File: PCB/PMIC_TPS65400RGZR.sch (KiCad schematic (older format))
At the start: 1 part

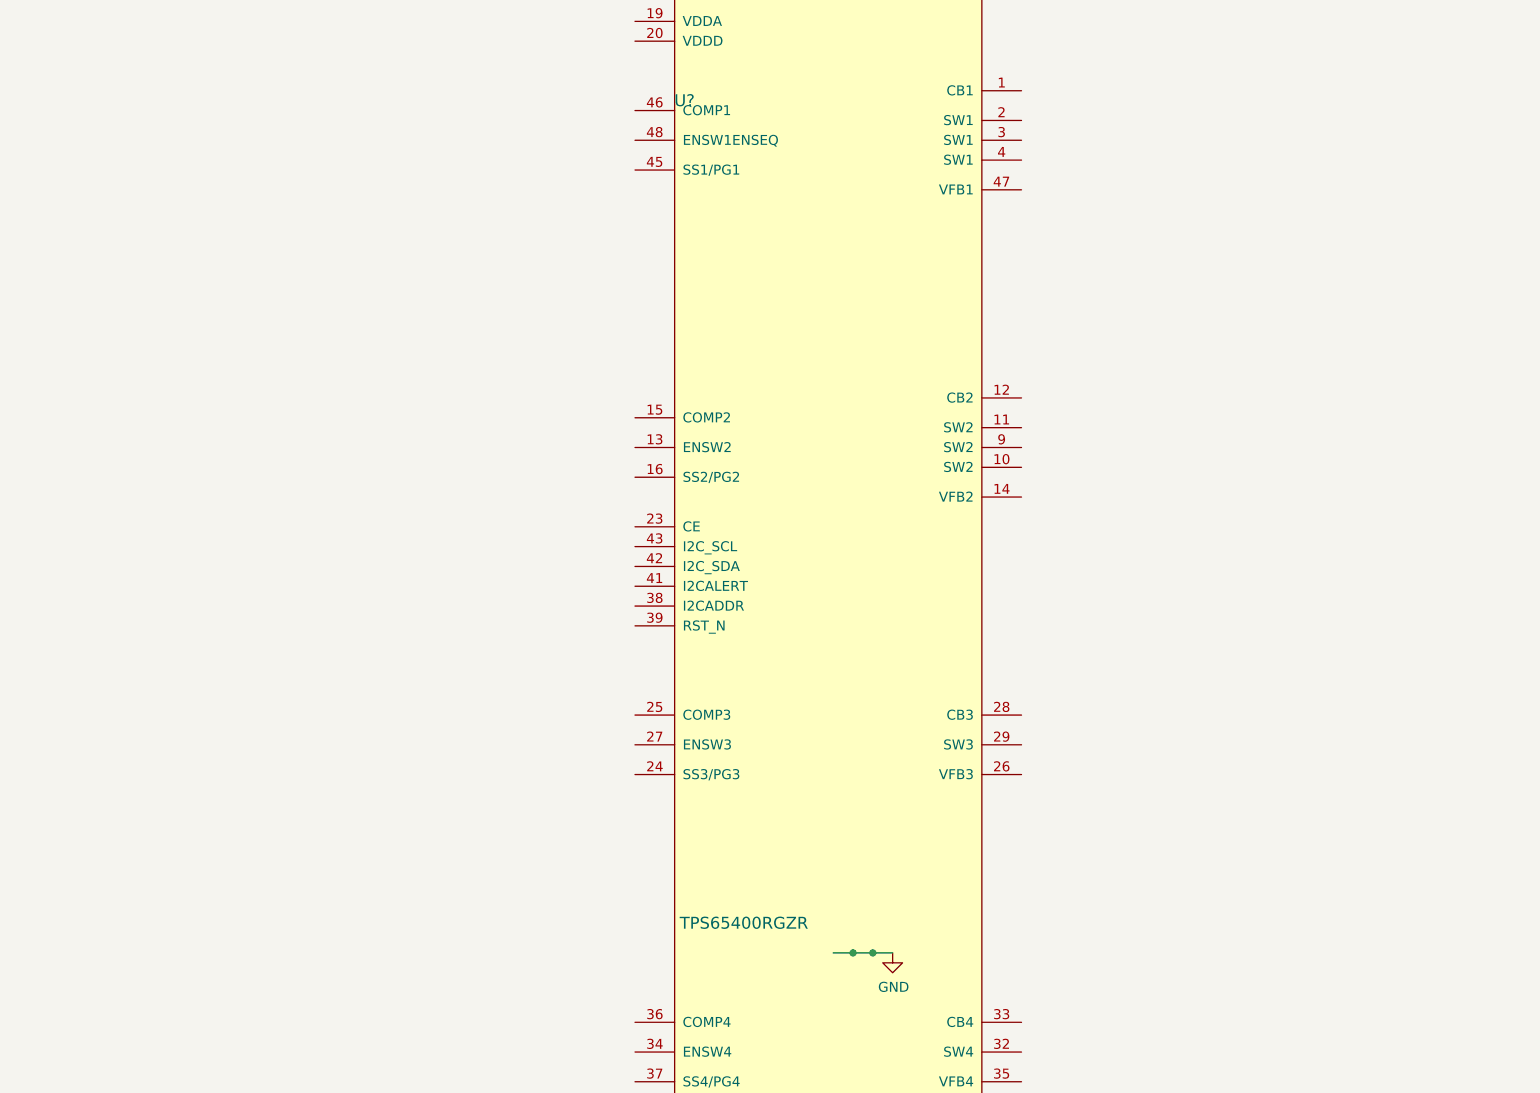
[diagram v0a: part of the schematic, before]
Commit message: PMIC progress
PMIC schematic implementation underway. will finish tomorrow evening
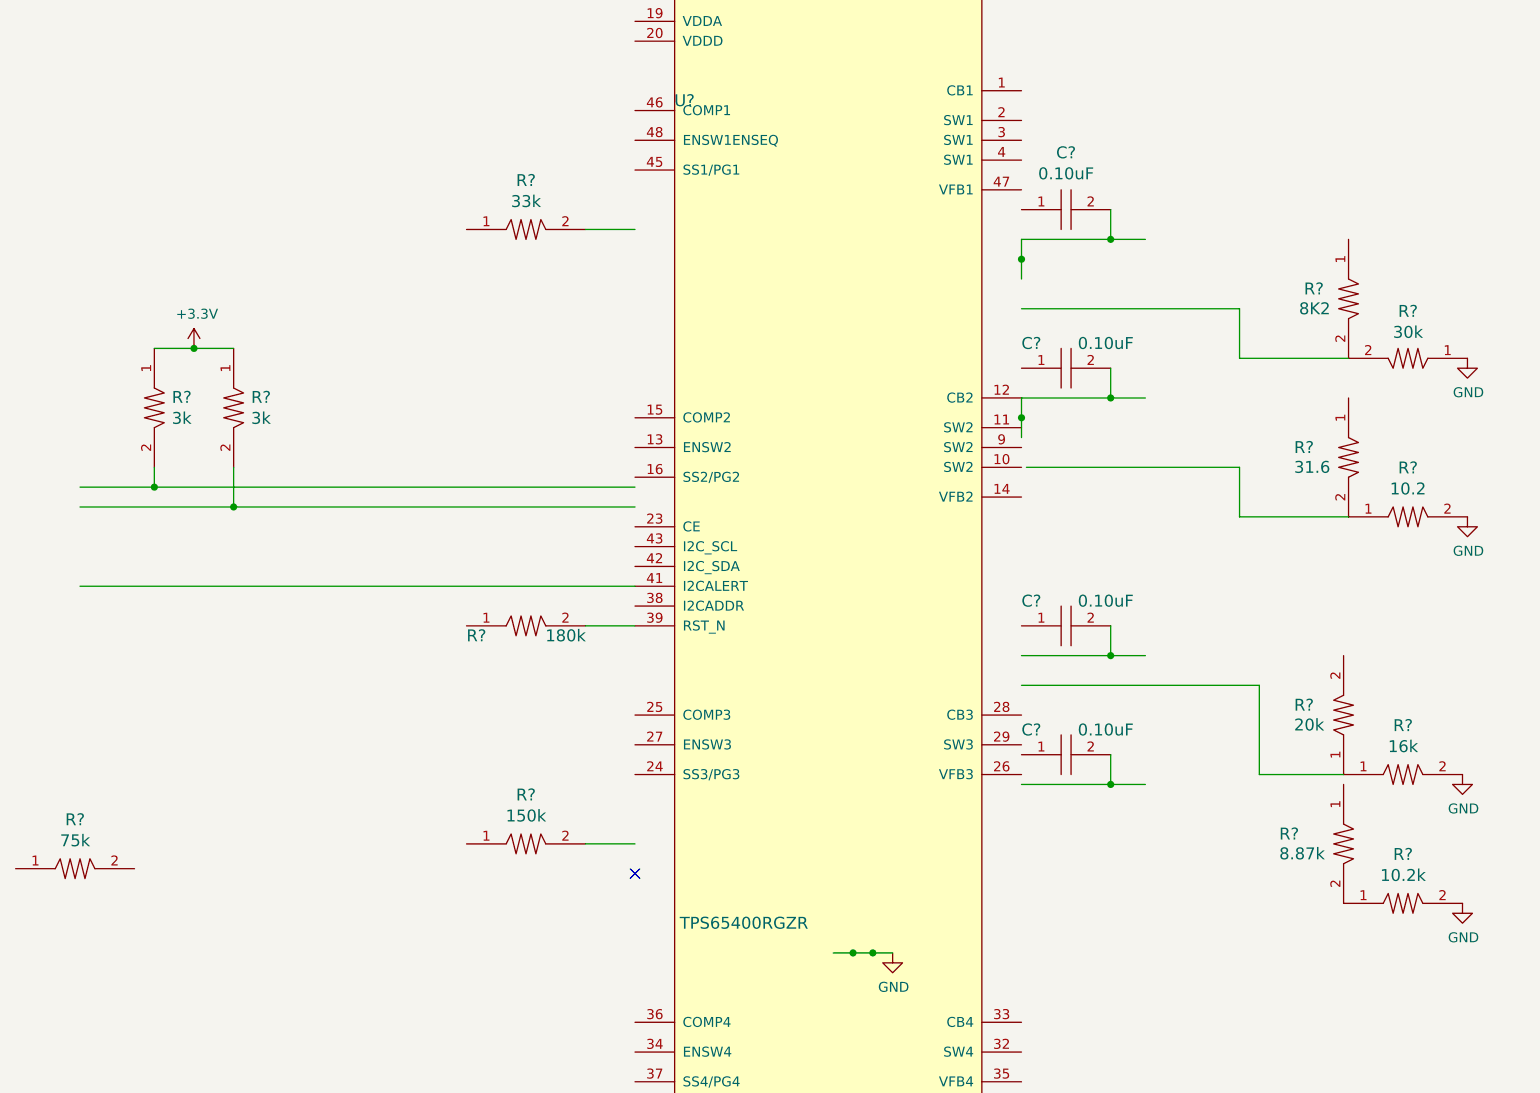
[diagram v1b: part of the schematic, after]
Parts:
- added C? (x4): CL05A104JO5NNNC, PCB_Footprints:C0402, symbol CL05A104JO5NNNC
- added R?: RC0402FR-0710K2L, PCB_Footprints:R0402, symbol RC0402FR-0710K2L
- added R?: RC0402FR-0710R2L, PCB_Footprints:R0402, symbol RC0402FR-0710R2L
- added R?: RC0402FR-07150KL, PCB_Footprints:R0402, symbol RC0402FR-07150KL
- added R?: RC0402FR-0716KL, PCB_Footprints:R0402, symbol RC0402FR-0716KL
- added R?: RC0402FR-07180KL, PCB_Footprints:R0402, symbol RC0402FR-07180KL
- added R?: RC0402FR-0720KL, PCB_Footprints:R0402, symbol RC0402FR-0720KL
- added R?: RC0402FR-0730KL, PCB_Footprints:R0402, symbol RC0402FR-0730KL
- added R?: RC0402FR-0731R6L, PCB_Footprints:R0402, symbol RC0402FR-0731R6L
- added R?: RC0402FR-0733KL, PCB_Footprints:R0402, symbol RC0402FR-0733KL
- added R? (x2): RC0402FR-073KL, PCB_Footprints:R0402, symbol RC0402FR-073KL
- added R?: RC0402FR-0775KL, PCB_Footprints:R0402, symbol RC0402FR-0775KL
- added R?: RC0402FR-078K2L, PCB_Footprints:R0402, symbol RC0402FR-078K2L
- added R?: RC0402FR-078K87L, PCB_Footprints:R0402, symbol RC0402FR-078K87L
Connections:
- net labels added: +3.3V
- wire segments 1 -> 39
- no-connect marks 0 -> 1

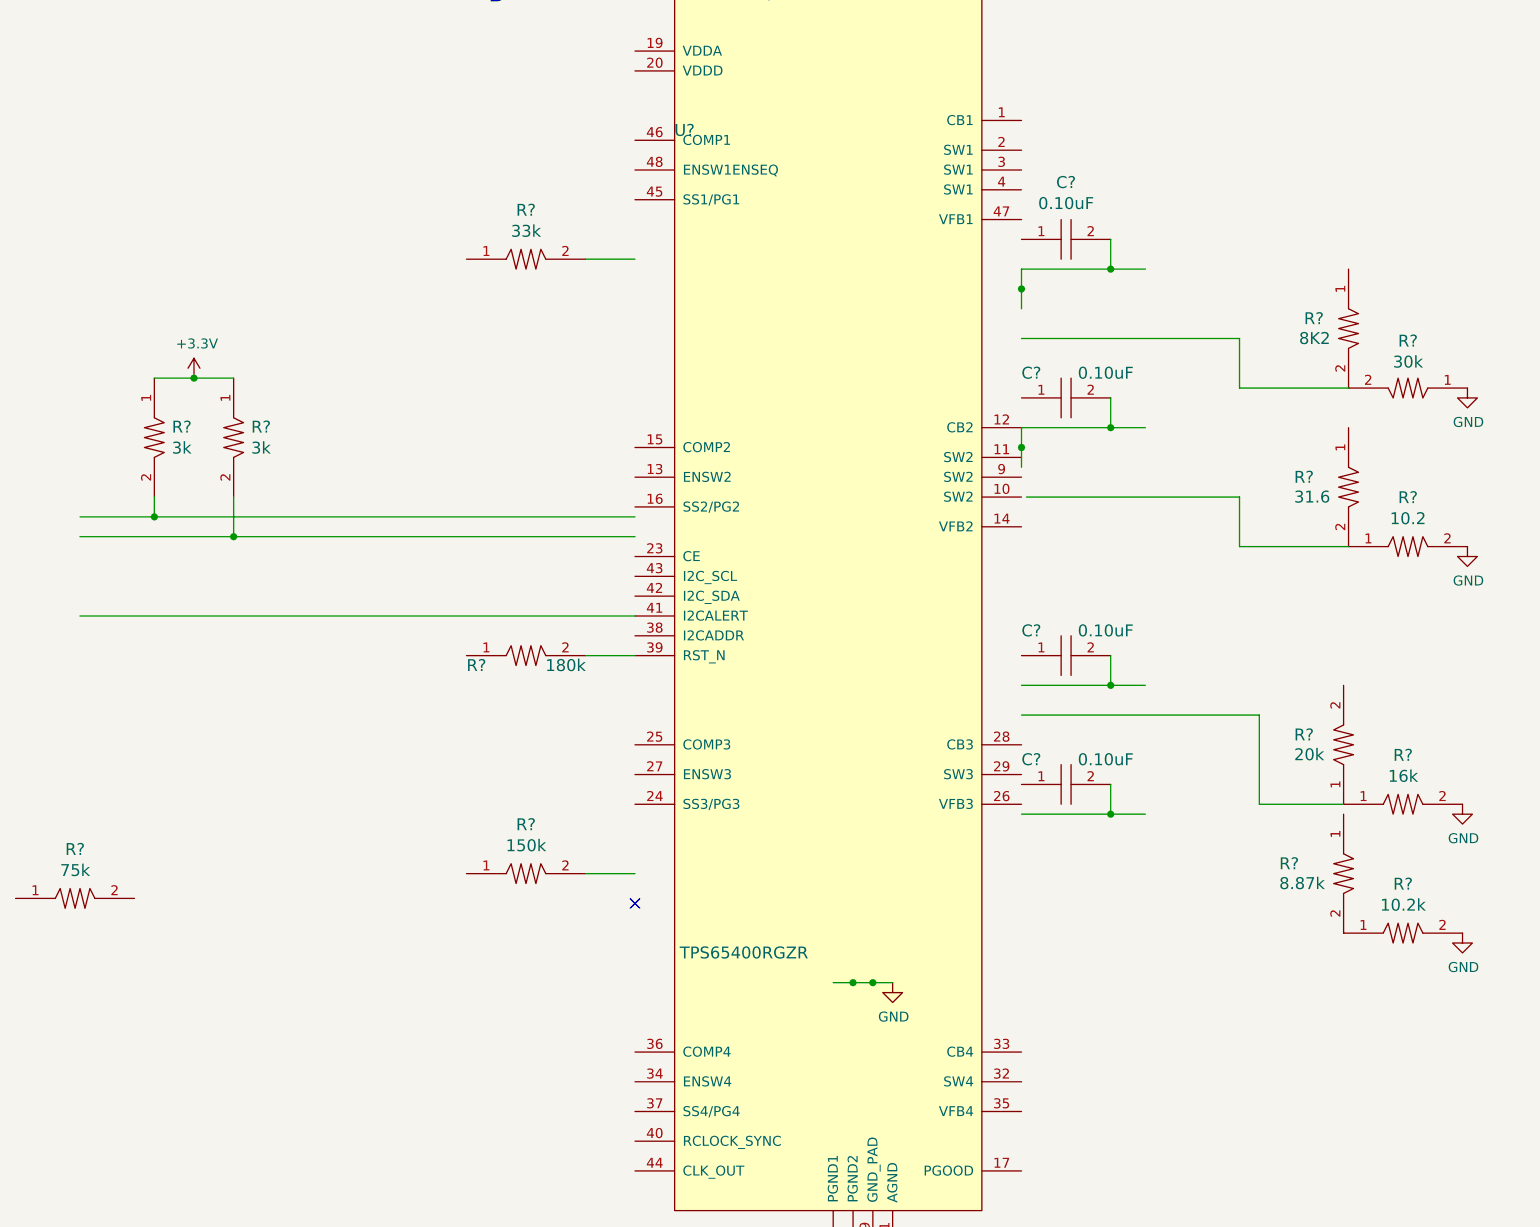
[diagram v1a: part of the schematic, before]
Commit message: PMIC
PMIC progress made, symbol revised for neater schematic. Components
selected and created in the footprints repo.
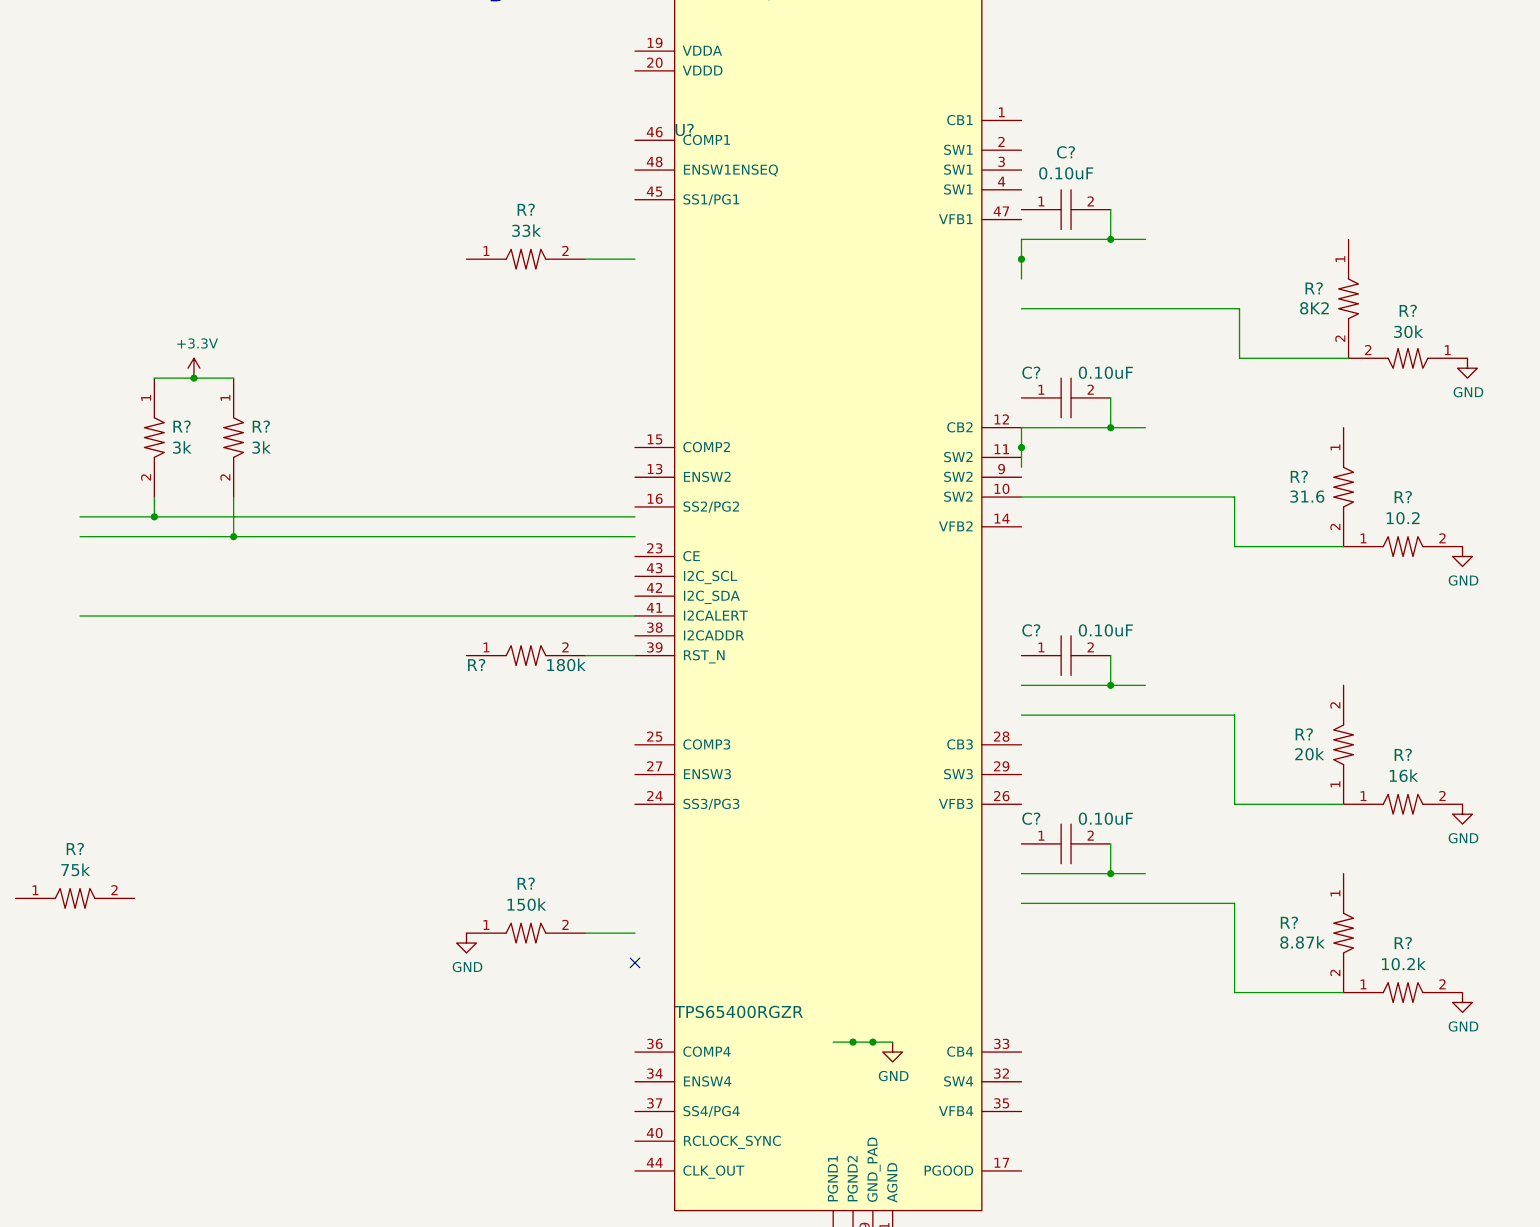
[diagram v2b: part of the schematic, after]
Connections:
- wire segments 39 -> 43
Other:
- moved on the sheet: C?, R?
